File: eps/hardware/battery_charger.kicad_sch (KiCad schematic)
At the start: 19 parts, among them Q1 NMOS, Q2 NMOS, U3 LTC4162-L

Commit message: netlist fixes
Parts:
- renumbered R24 to R12, R25 to R13, R26 to R14, R27 to R15, R28 to R16, R29 to R17
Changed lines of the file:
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@@
 		(on_board yes)
 		(dnp no)
-		(property "Reference" "R27"
+		(property "Reference" "R15"
 			(at 103.632 85.09 0)
 			(effects
@@
 			(project ""
 				(path "/9e0ae2e7-d4be-41b4-8312-0d2aceea2180/5908e624-b9d3-44ce-b527-44975367145b"
-					(reference "R33")
-					(unit 1)
-				)
-				(path "/9e0ae2e7-d4be-41b4-8312-0d2aceea2180/ae433a55-008e-45d6-9a90-c7b82ac6a9db"
-					(reference "R27")
+					(reference "R21")
+					(unit 1)
+				)
+				(path "/9e0ae2e7-d4be-41b4-8312-0d2aceea2180/ae433a55-008e-45d6-9a90-c7b82ac6a9db"
+					(reference "R15")
 					(unit 1)
 				)
@@
 		(on_board yes)
 		(dnp no)
-		(property "Reference" "R28"
+		(property "Reference" "R16"
 			(at 133.35 70.612 90)
 			(effects
@@
 			(project ""
 				(path "/9e0ae2e7-d4be-41b4-8312-0d2aceea2180/5908e624-b9d3-44ce-b527-44975367145b"
-					(reference "R34")
-					(unit 1)
-				)
-				(path "/9e0ae2e7-d4be-41b4-8312-0d2aceea2180/ae433a55-008e-45d6-9a90-c7b82ac6a9db"
-					(reference "R28")
+					(reference "R22")
+					(unit 1)
+				)
+				(path "/9e0ae2e7-d4be-41b4-8312-0d2aceea2180/ae433a55-008e-45d6-9a90-c7b82ac6a9db"
+					(reference "R16")
 					(unit 1)
 				)
@@
 		(on_board yes)
 		(dnp no)
-		(property "Reference" "R26"
+		(property "Reference" "R14"
 			(at 92.964 18.542 90)
 			(effects
@@
 			(project ""
 				(path "/9e0ae2e7-d4be-41b4-8312-0d2aceea2180/5908e624-b9d3-44ce-b527-44975367145b"
-					(reference "R32")
-					(unit 1)
-				)
-				(path "/9e0ae2e7-d4be-41b4-8312-0d2aceea2180/ae433a55-008e-45d6-9a90-c7b82ac6a9db"
-					(reference "R26")
+					(reference "R20")
+					(unit 1)
+				)
+				(path "/9e0ae2e7-d4be-41b4-8312-0d2aceea2180/ae433a55-008e-45d6-9a90-c7b82ac6a9db"
+					(reference "R14")
 					(unit 1)
 				)
@@
 		(on_board yes)
 		(dnp no)
-		(property "Reference" "R29"
+		(property "Reference" "R17"
 			(at 149.86 60.9599 0)
 			(effects
@@
 			(project ""
 				(path "/9e0ae2e7-d4be-41b4-8312-0d2aceea2180/5908e624-b9d3-44ce-b527-44975367145b"
-					(reference "R35")
-					(unit 1)
-				)
-				(path "/9e0ae2e7-d4be-41b4-8312-0d2aceea2180/ae433a55-008e-45d6-9a90-c7b82ac6a9db"
-					(reference "R29")
+					(reference "R23")
+					(unit 1)
+				)
+				(path "/9e0ae2e7-d4be-41b4-8312-0d2aceea2180/ae433a55-008e-45d6-9a90-c7b82ac6a9db"
+					(reference "R17")
 					(unit 1)
 				)
@@
 		(on_board yes)
 		(dnp no)
-		(property "Reference" "R24"
+		(property "Reference" "R12"
 			(at 34.29 60.9599 0)
 			(effects
@@
 			(project ""
 				(path "/9e0ae2e7-d4be-41b4-8312-0d2aceea2180/5908e624-b9d3-44ce-b527-44975367145b"
-					(reference "R30")
-					(unit 1)
-				)
-				(path "/9e0ae2e7-d4be-41b4-8312-0d2aceea2180/ae433a55-008e-45d6-9a90-c7b82ac6a9db"
-					(reference "R24")
+					(reference "R18")
+					(unit 1)
+				)
+				(path "/9e0ae2e7-d4be-41b4-8312-0d2aceea2180/ae433a55-008e-45d6-9a90-c7b82ac6a9db"
+					(reference "R12")
 					(unit 1)
 				)
@@
 		(on_board yes)
 		(dnp no)
-		(property "Reference" "R25"
+		(property "Reference" "R13"
 			(at 43.18 60.9599 0)
 			(effects
@@
 			(project "eps"
 				(path "/9e0ae2e7-d4be-41b4-8312-0d2aceea2180/5908e624-b9d3-44ce-b527-44975367145b"
-					(reference "R31")
-					(unit 1)
-				)
-				(path "/9e0ae2e7-d4be-41b4-8312-0d2aceea2180/ae433a55-008e-45d6-9a90-c7b82ac6a9db"
-					(reference "R25")
-					(unit 1)
-				)
+					(reference "R19")
+					(unit 1)
+				)
+				(path "/9e0ae2e7-d4be-41b4-8312-0d2aceea2180/ae433a55-008e-45d6-9a90-c7b82ac6a9db"
+					(reference "R13")
+					(unit 1)
+				)

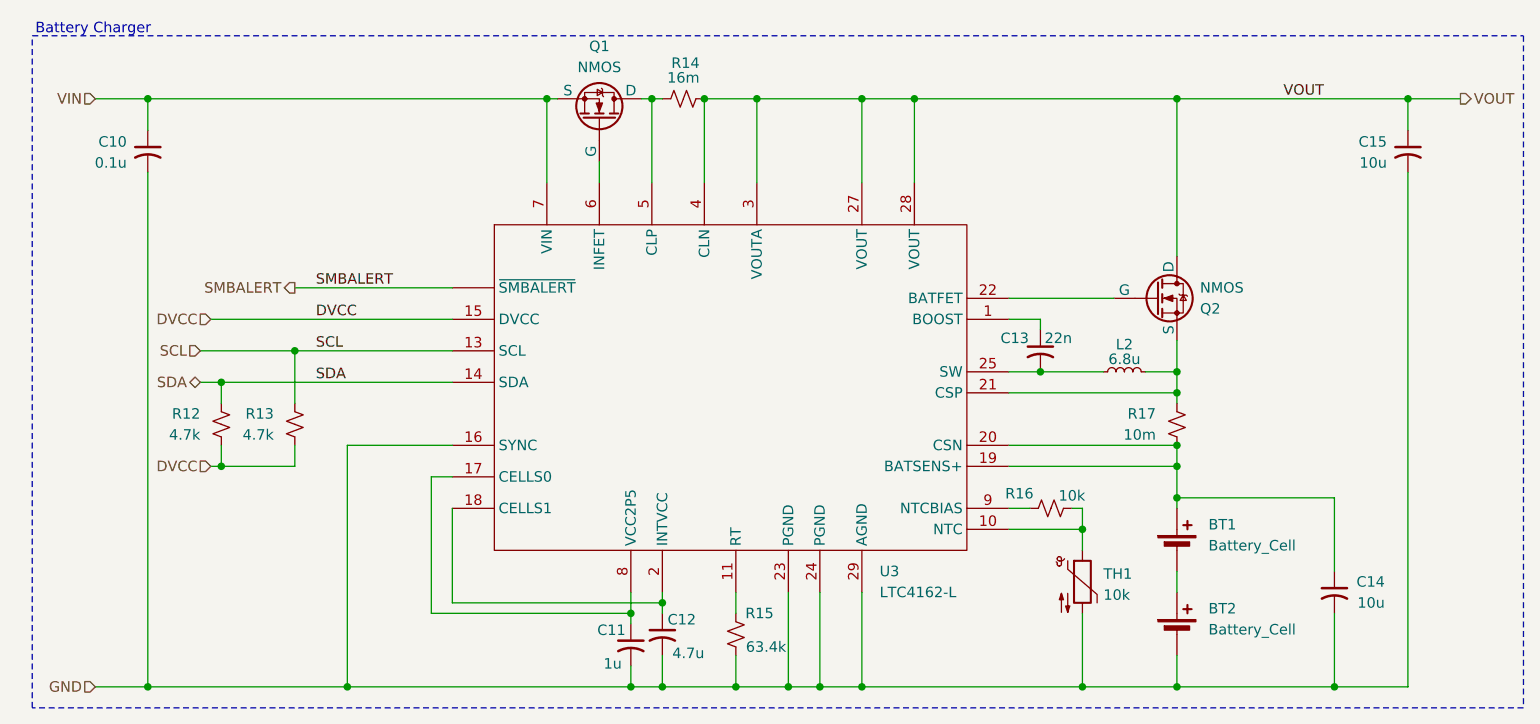
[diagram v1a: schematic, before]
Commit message: change battery cells to connector
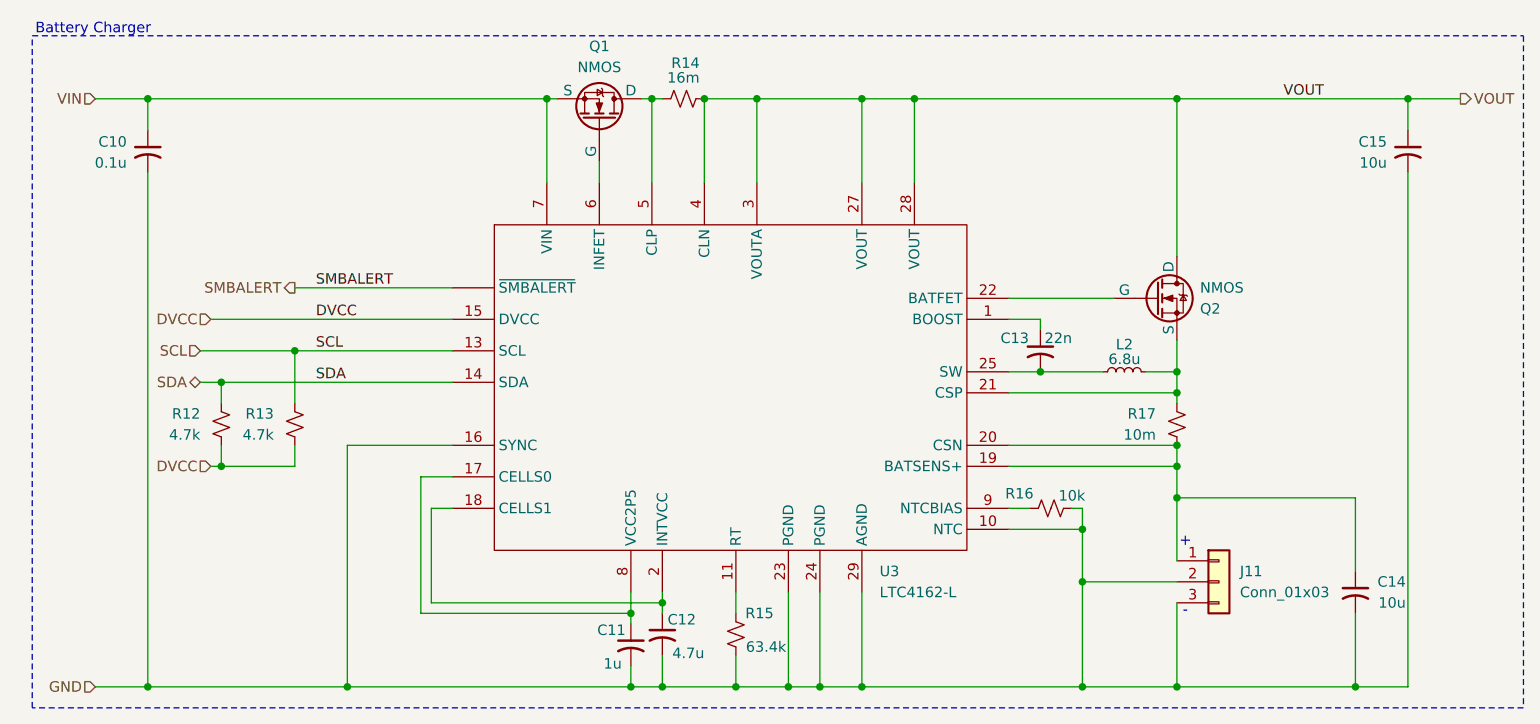
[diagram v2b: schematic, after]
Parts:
- removed BT1, BT2: Battery_Cell, symbol Device:Battery_Cell
- removed TH1: 10k, symbol Device:Thermistor_NTC
- added J11: Conn_01x03, symbol Connector_Generic:Conn_01x03
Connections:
- net GND: now also R16.2, U3.10 (NTC), J11.2 (Pin_2), J11.3 (Pin_3)
- net at C14.1, R17.2, U3.19 (BATSENS+)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: now also J11.1 (Pin_1)
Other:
- note added: "+"
- note added: "-"
- moved on the sheet: C14

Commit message: start footprint assignment
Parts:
- C10, C11, C12, C13, C14, C15: footprint (none) -> Capacitor_SMD:C_0603_1608Metric
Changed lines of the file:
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@@
 			)
 		)
-		(property "Footprint" ""
+		(property "Footprint" "Capacitor_SMD:C_0603_1608Metric"
 			(at 90.17 87.63 0)
 			(effects
@@
 			)
 		)
-		(property "Footprint" ""
+		(property "Footprint" "Capacitor_SMD:C_0603_1608Metric"
 			(at 173.99 82.55 0)
 			(effects
@@
 			)
 		)
-		(property "Footprint" ""
+		(property "Footprint" "Capacitor_SMD:C_0603_1608Metric"
 			(at 180.34 29.21 0)
 			(effects
@@
 			)
 		)
-		(property "Footprint" ""
+		(property "Footprint" "Capacitor_SMD:C_0603_1608Metric"
 			(at 135.89 53.34 0)
 			(effects
@@
 			)
 		)
-		(property "Footprint" ""
+		(property "Footprint" "Capacitor_SMD:C_0603_1608Metric"
 			(at 86.36 88.9 0)
 			(effects
@@
 			)
 		)
-		(property "Footprint" ""
+		(property "Footprint" "Capacitor_SMD:C_0603_1608Metric"
 			(at 27.94 29.21 0)
 			(effects

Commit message: finish footprint assignment and board setup
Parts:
- J11: footprint (none) -> Connector_JST:JST_PH_S3B-PH-K_1x03_P2.00mm_Horizontal
- L2: footprint (none) -> Inductor_SMD:L_Vishay_IHLP-2020
- Q1, Q2: footprint (none) -> Package_TO_SOT_SMD:SOT-23-3
- R12, R13, R14, R15, R16, R17: footprint (none) -> Resistor_SMD:R_0603_1608Metric
- U3: footprint (none) -> Package_DFN_QFN:QFN-28-1EP_4x5mm_P0.5mm_EP2.65x3.65mm
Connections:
- net SMBALERT: now also U3.12 (~{SMBALERT}); no longer U3. (~{SMBALERT})
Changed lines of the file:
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@@
 			)
 		)
-		(property "Footprint" ""
+		(property "Footprint" "Resistor_SMD:R_0603_1608Metric"
 			(at 99.06 87.63 0)
 			(effects
@@
 			)
 		)
-		(property "Footprint" ""
+		(property "Footprint" "Connector_JST:JST_PH_S3B-PH-K_1x03_P2.00mm_Horizontal"
 			(at 157.48 81.28 0)
 			(effects
@@
 			)
 		)
-		(property "Footprint" ""
+		(property "Footprint" "Inductor_SMD:L_Vishay_IHLP-2020"
 			(at 146.05 55.88 0)
 			(effects
@@
 			)
 		)
-		(property "Footprint" ""
+		(property "Footprint" "Resistor_SMD:R_0603_1608Metric"
 			(at 137.16 72.39 0)
 			(effects
@@
 			)
 		)
-		(property "Footprint" ""
+		(property "Footprint" "Package_TO_SOT_SMD:SOT-23-3"
 			(at 154.94 44.45 0)
 			(effects
@@
 			)
 		)
-		(property "Footprint" ""
+		(property "Footprint" "Resistor_SMD:R_0603_1608Metric"
 			(at 92.71 22.86 0)
 			(effects
@@
 			)
 		)
-		(property "Footprint" ""
+		(property "Footprint" "Resistor_SMD:R_0603_1608Metric"
 			(at 152.4 62.23 0)
 			(effects
@@
 			)
 		)
-		(property "Footprint" ""
+		(property "Footprint" "Package_TO_SOT_SMD:SOT-23-3"
 			(at 85.09 20.32 0)
 			(effects
@@
 			)
 		)
-		(property "Footprint" ""
+		(property "Footprint" "Resistor_SMD:R_0603_1608Metric"
 			(at 36.83 62.23 0)
 			(effects
@@
 			)
 		)
-		(property "Footprint" ""
+		(property "Footprint" "Resistor_SMD:R_0603_1608Metric"
 			(at 45.72 62.23 0)
 			(effects
@@
 			)
 		)
-		(property "Footprint" ""
+		(property "Footprint" "Package_DFN_QFN:QFN-28-1EP_4x5mm_P0.5mm_EP2.65x3.65mm"
 			(at 99.06 33.02 0)
 			(effects
@@
 		(pin "27"
 		)
-		(pin ""
+		(pin "12"
 		)
 		(pin "3"

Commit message: fix update errors
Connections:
- net at C13.2, L2.1, U3.25 (SW): now also U3.26 (SW)
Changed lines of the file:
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@@
 		(pin "25"
+		)
+		(pin "26"
 		)
 		(instances

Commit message: schematic fixes
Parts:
- C10, C11, C12, C13, C14, C15: footprint Capacitor_SMD:C_0603_1608Metric -> Capacitor_SMD:C_0402_1005Metric
- R12, R13, R14, R15, R16, R17: footprint Resistor_SMD:R_0603_1608Metric -> Resistor_SMD:R_0402_1005Metric
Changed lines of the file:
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@@
 			)
 		)
-		(property "Footprint" "Resistor_SMD:R_0603_1608Metric"
+		(property "Footprint" "Resistor_SMD:R_0402_1005Metric"
 			(at 99.06 87.63 0)
 			(effects
@@
 			)
 		)
-		(property "Footprint" "Resistor_SMD:R_0603_1608Metric"
+		(property "Footprint" "Resistor_SMD:R_0402_1005Metric"
 			(at 137.16 72.39 0)
 			(effects
@@
 			)
 		)
-		(property "Footprint" "Capacitor_SMD:C_0603_1608Metric"
+		(property "Footprint" "Capacitor_SMD:C_0402_1005Metric"
 			(at 90.17 87.63 0)
 			(effects
@@
 			)
 		)
-		(property "Footprint" "Resistor_SMD:R_0603_1608Metric"
+		(property "Footprint" "Resistor_SMD:R_0402_1005Metric"
 			(at 92.71 22.86 0)
 			(effects
@@
 			)
 		)
-		(property "Footprint" "Resistor_SMD:R_0603_1608Metric"
+		(property "Footprint" "Resistor_SMD:R_0402_1005Metric"
 			(at 152.4 62.23 0)
 			(effects
@@
 			)
 		)
-		(property "Footprint" "Resistor_SMD:R_0603_1608Metric"
+		(property "Footprint" "Resistor_SMD:R_0402_1005Metric"
 			(at 36.83 62.23 0)
 			(effects
@@
 			)
 		)
-		(property "Footprint" "Capacitor_SMD:C_0603_1608Metric"
+		(property "Footprint" "Capacitor_SMD:C_0402_1005Metric"
 			(at 173.99 82.55 0)
 			(effects
@@
 			)
 		)
-		(property "Footprint" "Capacitor_SMD:C_0603_1608Metric"
+		(property "Footprint" "Capacitor_SMD:C_0402_1005Metric"
 			(at 180.34 29.21 0)
 			(effects
@@
 			)
 		)
-		(property "Footprint" "Capacitor_SMD:C_0603_1608Metric"
+		(property "Footprint" "Capacitor_SMD:C_0402_1005Metric"
 			(at 135.89 53.34 0)
 			(effects
@@
 			)
 		)
-		(property "Footprint" "Resistor_SMD:R_0603_1608Metric"
+		(property "Footprint" "Resistor_SMD:R_0402_1005Metric"
 			(at 45.72 62.23 0)
 			(effects
@@
 			)
 		)
-		(property "Footprint" "Capacitor_SMD:C_0603_1608Metric"
+		(property "Footprint" "Capacitor_SMD:C_0402_1005Metric"
 			(at 86.36 88.9 0)
 			(effects
@@
 			)
 		)
-		(property "Footprint" "Capacitor_SMD:C_0603_1608Metric"
+		(property "Footprint" "Capacitor_SMD:C_0402_1005Metric"
 			(at 27.94 29.21 0)
 			(effects

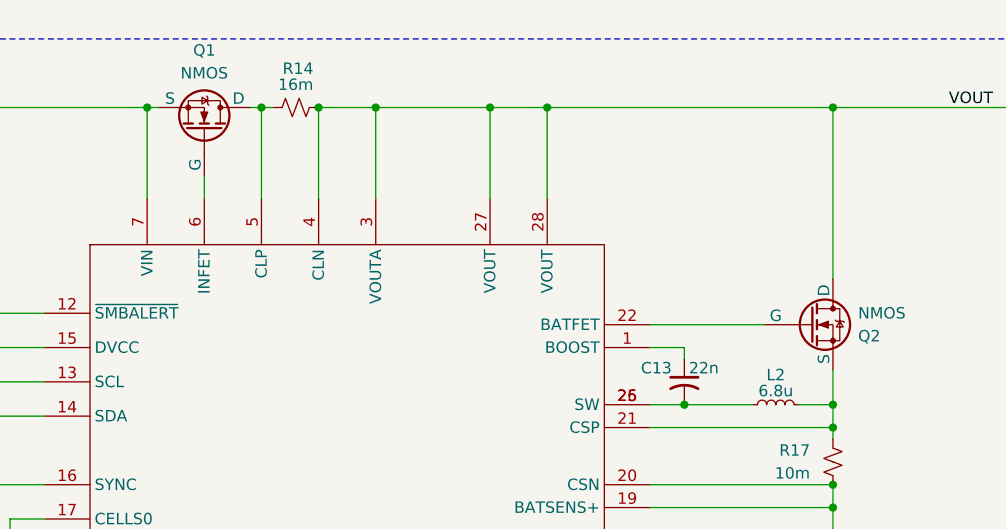
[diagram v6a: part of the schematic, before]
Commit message: fix all obvious schematic issues
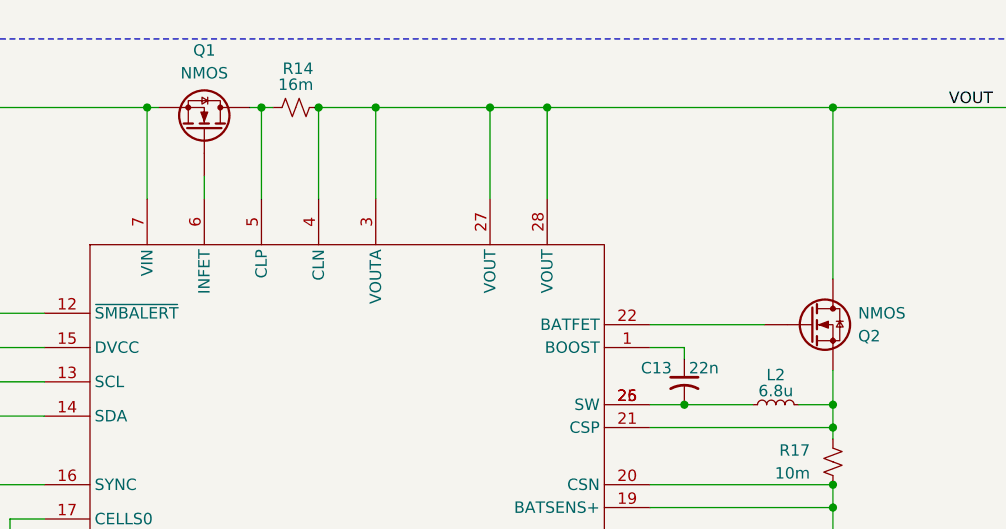
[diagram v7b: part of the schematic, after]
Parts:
- Q1, Q2: footprint Package_TO_SOT_SMD:SOT-23-3 -> footprints:TRANS_FDMC8327L; symbol Simulation_SPICE:NMOS -> Device:Q_NMOS
- R14: footprint Resistor_SMD:R_0402_1005Metric -> Resistor_SMD:R_1206_3216Metric
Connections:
- net VIN: now also Q1.5 (S), Q1.6 (S), Q1.7 (S), Q1.8 (S), Q1.9 (S); no longer Q1.3 (S)
- net VOUT: now also Q2.2 (D), Q2.3 (D)
- net at L2.2, R17.1, U3.21 (CSP): now also Q2.5 (S), Q2.6 (S), Q2.7 (S), Q2.8 (S), Q2.9 (S); no longer Q2.3 (S)
- net at U3.22 (BATFET): now also Q2.4 (G); no longer Q2.2 (G)
- net at Q1.1 (D), R14.1, U3.5 (CLP): now also Q1.2 (D), Q1.3 (D)
- net at U3.6 (INFET): now also Q1.4 (G); no longer Q1.2 (G)
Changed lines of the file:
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@@
 	)
 	(symbol
-		(lib_id "Simulation_SPICE:NMOS")
+		(lib_id "Device:Q_NMOS")
 		(at 149.86 46.99 0)
 		(unit 1)
@@
 			)
 		)
-		(property "Footprint" "Package_TO_SOT_SMD:SOT-23-3"
+		(property "Footprint" "footprints:TRANS_FDMC8327L"
 			(at 154.94 44.45 0)
 			(effects
@@
 			)
 		)
-		(property "Datasheet" "https://ngspice.sourceforge.io/docs/ngspice-html-manual/manual.xhtml#cha_MOSFETs"
-			(at 149.86 59.69 0)
-			(effects
-				(font
-					(size 1.27 1.27)
-				)
-				(hide yes)
-			)
-		)
-		(property "Description" "N-MOSFET transistor, drain/source/gate"
+		(property "Datasheet" "~"
+			(at 149.86 46.99 0)
+			(effects
+				(font
+					(size 1.27 1.27)
+				)
+				(hide yes)
+			)
+		)
+		(property "Description" "N-MOSFET transistor"
 			(at 149.86 46.99 0)
 			(effects
@@
 			)
 		)
+		(pin "5"
+		)
+		(pin "1"
+		)
+		(pin "6"
+		)
+		(pin "7"
+		)
+		(pin "9"
+		)
+		(pin "2"
+		)
+		(pin "4"
+		)
+		(pin "8"
+		)
 		(pin "3"
-		)
-		(pin "1"
-		)
-		(pin "2"
 		)
 		(instances
@@
 			)
 		)
-		(property "Footprint" "Resistor_SMD:R_0402_1005Metric"
+		(property "Footprint" "Resistor_SMD:R_1206_3216Metric"
 			(at 92.71 22.86 0)
 			(effects
@@
 	)
 	(symbol
-		(lib_id "Simulation_SPICE:NMOS")
+		(lib_name "Q_NMOS_1")
+		(lib_id "Device:Q_NMOS")
 		(at 82.55 25.4 270)
 		(mirror x)
@@
 			)
 		)
-		(property "Footprint" "Package_TO_SOT_SMD:SOT-23-3"
+		(property "Footprint" "footprints:TRANS_FDMC8327L"
 			(at 85.09 20.32 0)
 			(effects
@@
 			)
 		)
-		(property "Datasheet" "https://ngspice.sourceforge.io/docs/ngspice-html-manual/manual.xhtml#cha_MOSFETs"
-			(at 69.85 25.4 0)
-			(effects
-				(font
-					(size 1.27 1.27)
-				)
-				(hide yes)
-			)
-		)
-		(property "Description" "N-MOSFET transistor, drain/source/gate"
+		(property "Datasheet" "~"
+			(at 82.55 25.4 0)
+			(effects
+				(font
+					(size 1.27 1.27)
+				)
+				(hide yes)
+			)
+		)
+		(property "Description" "N-MOSFET transistor"
 			(at 82.55 25.4 0)
 			(effects
@@
 			)
 		)
+		(pin "4"
+		)
+		(pin "7"
+		)
+		(pin "1"
+		)
+		(pin "2"
+		)
 		(pin "3"
 		)
-		(pin "1"
-		)
-		(pin "2"
+		(pin "9"
+		)
+		(pin "8"
+		)
+		(pin "6"
+		)
+		(pin "5"
 		)
 		(instances

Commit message: optimize battery charger layout
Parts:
- C15: footprint Capacitor_SMD:C_0402_1005Metric -> Capacitor_SMD:C_1206_3216Metric
